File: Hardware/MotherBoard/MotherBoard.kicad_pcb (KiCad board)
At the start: 2 copper layers, 145 x 160 mm, 55 parts, among them J1 POWER, J10 I/O_PWR, J11 DMA_PULLUP, J12 NMI_PULLUP, J13 USB_OTG, J14 IRQ0_PULLUP, J2 I/O0, J3 ISA1, J4 ISA0, J5 I/O1, J6 EXTRN_CLCK, J9 Conn_02x02_Odd_Even, SW1 RESET_SW, SW2 ON_OFF, U1 AMS1117-5.0, U10 74HC245, U11 74HC245, U12 74HC245, U13 74HC541, U14 74HC541, U2 AT28C256, U3 WD65C22, U4 AS6C62256, U5 WD65C02, U6 74HC148, U7 74HC574, U8 ATF22V10B, U9 74HC245, X1 ACO-1MHz

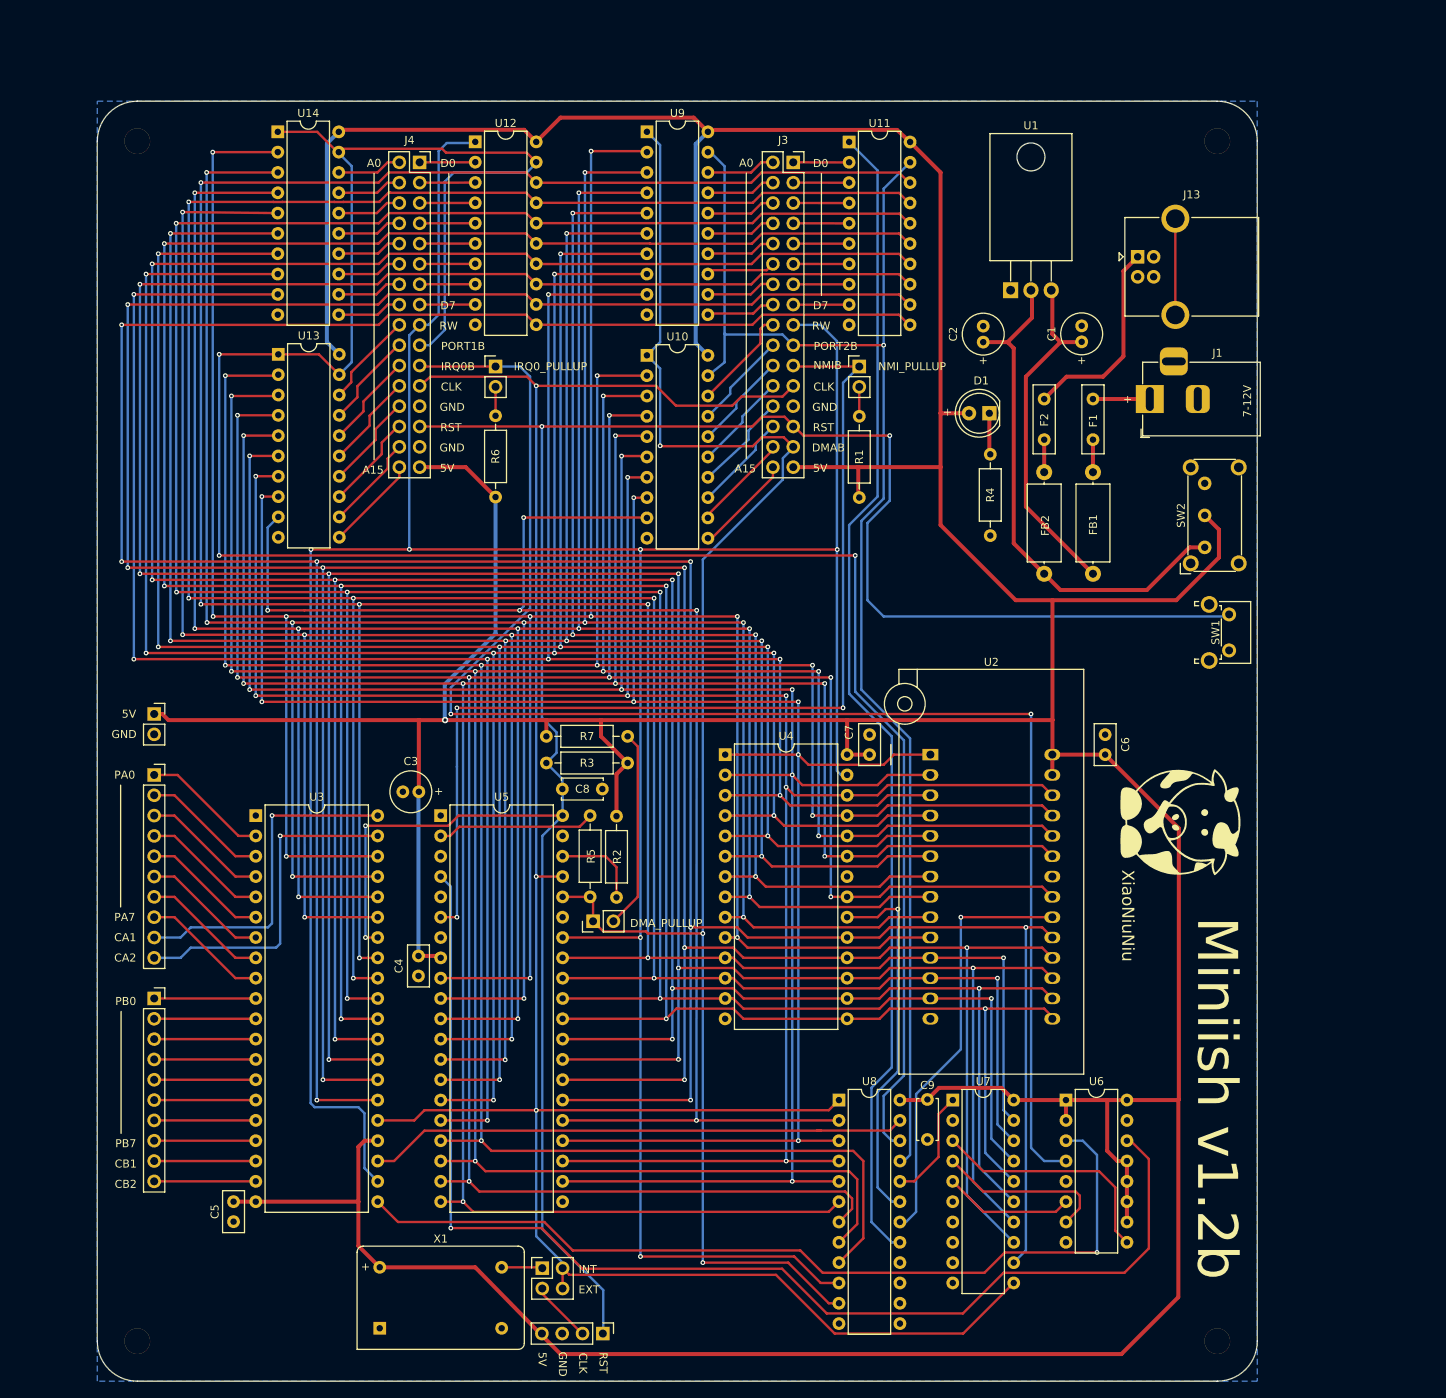
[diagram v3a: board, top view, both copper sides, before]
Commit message: Fix Reset, WAI Signal, Add PROG jumper and reformat luc files
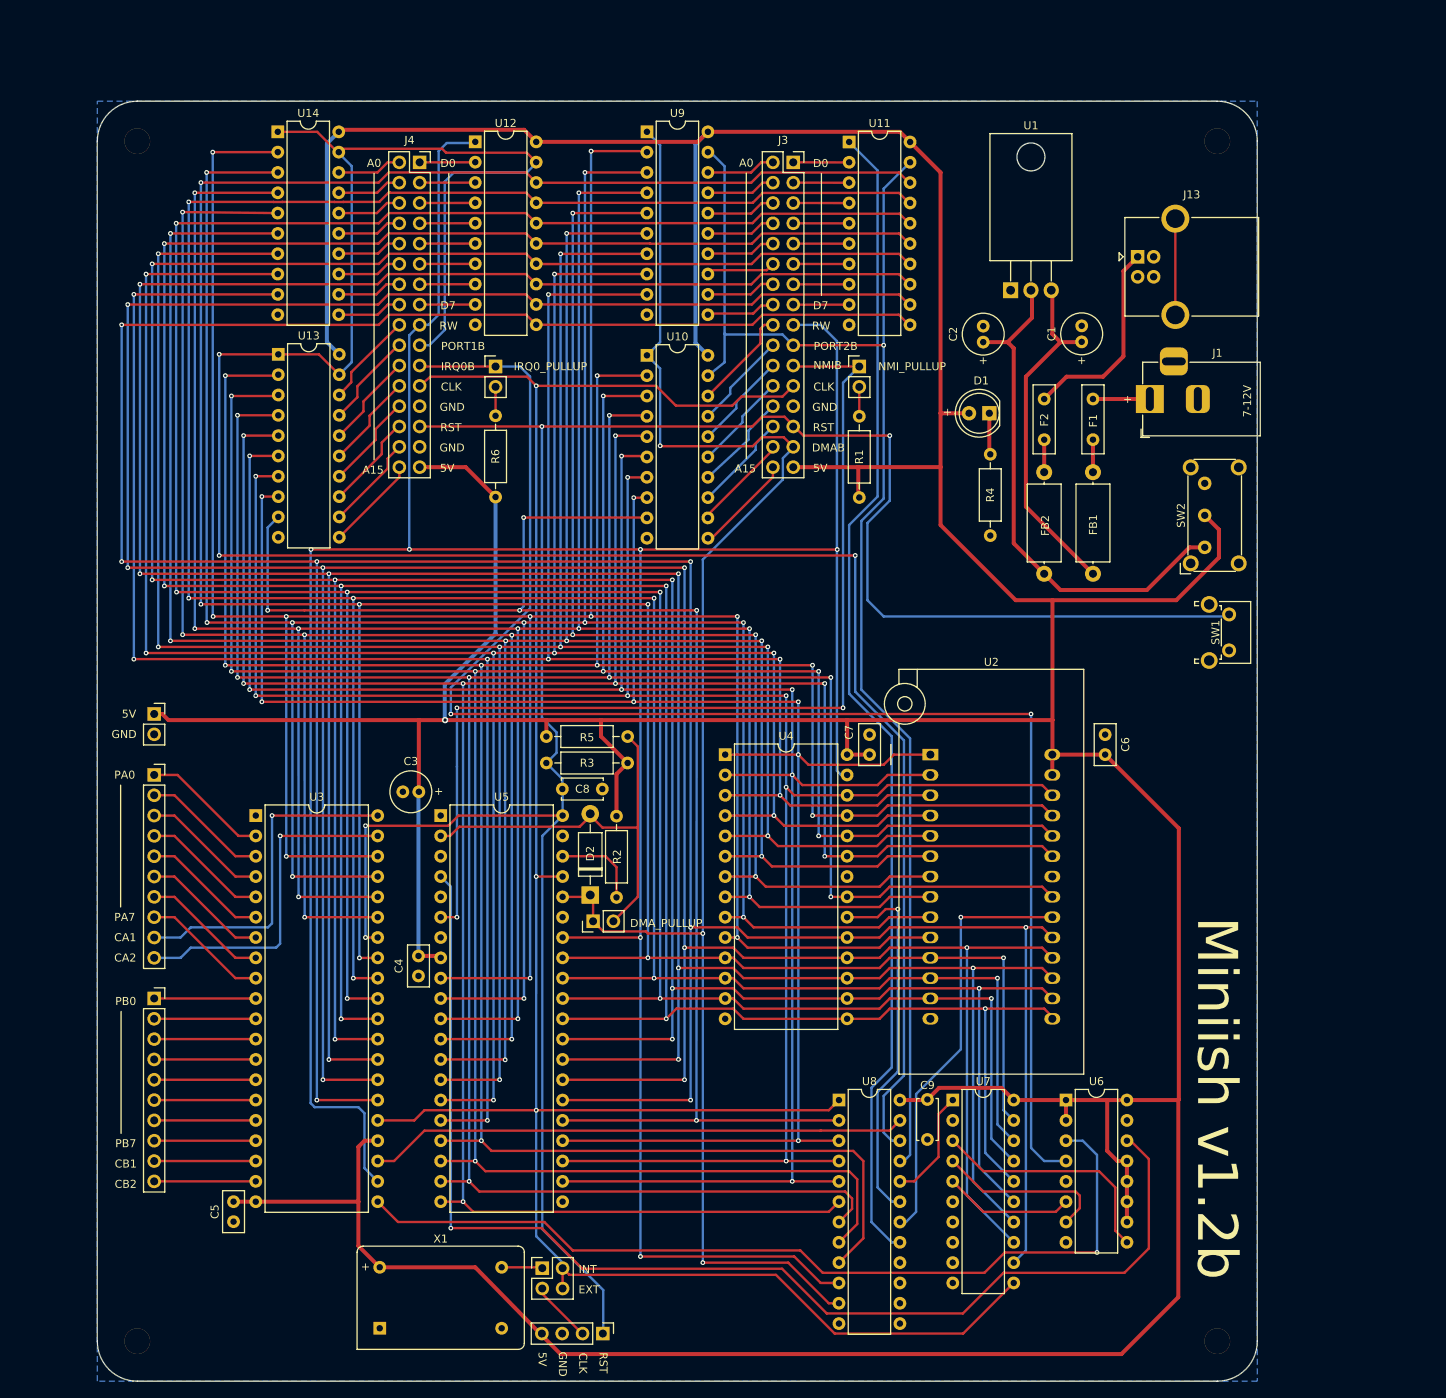
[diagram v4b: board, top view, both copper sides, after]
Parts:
- removed R7: 10K, Resistor_THT:R_Axial_DIN0207_L6.3mm_D2.5mm_P10.16mm_Horizontal
- removed XiaoNiuNiu: LOGO, Logos:SmallCow
- added D2: 1N4001, Diode_THT:D_DO-41_SOD81_P10.16mm_Horizontal, F.Cu at (84.8, 124.4)
- R1, R2, R5, R6: value 10K -> 3K3
- moved R5 10.9 mm to (89.5, 104.6), turned to 180 degrees
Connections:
- net /DMARW renamed /North Bridge/DMARW
- net /IOCSB renamed /Main /IOCSB
- net /IRQ0B renamed /North Bridge/IRQ0B
- net /IRQ1B renamed /Main /IRQ1B
- net /IRQB renamed /Main /IRQB
- net /NMIB renamed /Main /NMIB
- net /PORT1B renamed /North Bridge/PORT1B
- net /PORT2B renamed /North Bridge/PORT2B
- net /RAMCSB renamed /Main /RAMCSB
- net /ROMCSB renamed /Main /ROMCSB
- net /RW renamed /Main /RW
- J11 pad 1: /DMAB -> /Main /DMAB
- J11 pad 2: Net-(J11-Pad2) -> /Main /RDY
- J13 pad 2: (no net) -> unconnected-(J13-Pad2)
- J13 pad 3: (no net) -> unconnected-(J13-Pad3)
- J13 pad 5: no_connect_129 -> unconnected-(J13-Pad5)
- J3 pad 15: /DMAB -> /Main /DMAB
- R5 pad 1: Net-(R5-Pad1) -> /Main /RDY
- R5 pad 2: /DMAB -> +5V
- U10 pad 1: /DMAB -> /Main /DMAB
- U5 pad 1: (no net) -> unconnected-(U5-Pad1)
- U5 pad 2: Net-(R5-Pad1) -> /Main /RDY
- U5 pad 3: (no net) -> unconnected-(U5-Pad3)
- U5 pad 35: (no net) -> unconnected-(U5-Pad35)
- U5 pad 36: /DMAB -> /Main /DMAB
- U5 pad 39: (no net) -> unconnected-(U5-Pad39)
- U5 pad 5: (no net) -> unconnected-(U5-Pad5)
- U5 pad 7: (no net) -> unconnected-(U5-Pad7)
- U6 pad 15: (no net) -> unconnected-(U6-Pad15)
- U8 pad 11: /DMAB -> /Main /DMAB
- U8 pad 14: (no net) -> unconnected-(U8-Pad14)
- U8 pad 15: (no net) -> unconnected-(U8-Pad15)
- U8 pad 16: (no net) -> unconnected-(U8-Pad16)
- U9 pad 1: /DMAB -> /Main /DMAB
- X1 pad 1: (no net) -> unconnected-(X1-Pad1)
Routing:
- net /Main /DMAB: track 0.00 -> 205.7 mm, vias 0 -> 3
- net /DMAB: track 205.7 -> 0.00 mm, vias 3 -> 0
- net /Main /RDY: track 0.00 -> 51.2 mm
- net Net-(J11-Pad2): track 24.9 -> 0.00 mm
- net Net-(R5-Pad1): track 19.7 -> 0.00 mm
- net unconnected-(J13-Pad5): track 0.00 -> 12.0 mm
- net no_connect_129: track 12.0 -> 0.00 mm
- net +5V: track 762.0 -> 760.2 mm

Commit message: Cleanup and update version
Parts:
- added XiaoNiuNiu: LOGO, Logos:SmallCow, F.Cu at (39.5, 176.1)
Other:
- board text added: "Miniish v1.2c"
- board text removed: "Miniish v1.2b"

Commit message: New motherboard version
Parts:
- removed J1: POWER, Connector_BarrelJack:BarrelJack_Horizontal
- removed J10: I/O_PWR, Connector_PinSocket_2.54mm:PinSocket_1x02_P2.54mm_Vertical
- removed J11: DMA_PULLUP, Connector_PinHeader_2.54mm:PinHeader_1x02_P2.54mm_Vertical
- removed J12: NMI_PULLUP, Connector_PinHeader_2.54mm:PinHeader_1x02_P2.54mm_Vertical
- removed J13: USB_OTG, Connector_USB:USB_B_OST_USB-B1HSxx_Horizontal
- removed J2: I/O0, Connector_PinSocket_2.54mm:PinSocket_1x10_P2.54mm_Vertical
- removed J5: I/O1, Connector_PinSocket_2.54mm:PinSocket_1x10_P2.54mm_Vertical
- removed J6: EXTRN_CLCK, Connector_PinHeader_2.54mm:PinHeader_1x04_P2.54mm_Vertical
- removed J9: Conn_02x02_Odd_Even, Connector_PinHeader_2.54mm:PinHeader_2x02_P2.54mm_Vertical
- removed SW1: RESET_SW, Button_Switch_THT:SW_Tactile_SPST_Angled_PTS645Vx83-2LFS
- removed SW2: ON_OFF, Button_Switch_THT:SW_E-Switch_EG1224_SPDT_Angled
- removed U10, U11, U12: 74HC245, Package_DIP:DIP-20_W7.62mm
- removed U13, U14: 74HC541, Package_DIP:DIP-20_W7.62mm
- removed X1: ACO-1MHz, Oscillator:Oscillator_DIP-14
- removed the XiaoNiuNiu at (39.5, 176.1)
- added +12V: POWER, Connector_BarrelJack:BarrelJack_Horizontal, F.Cu at (147.7, 28.8)
- added +5V: USB_OTG, Connector_USB:USB_B_OST_USB-B1HSxx_Horizontal, F.Cu at (161.6, 30.7)
- added 16MHz: ACO-16MHz, Oscillator:Oscillator_DIP-14, F.Cu at (40.3, 144.7)
- added C10: 100nF, Capacitor_THT:C_Disc_D5.0mm_W2.5mm_P2.50mm, F.Cu at (55.6, 101.6)
- added C11: 100nF, Capacitor_THT:C_Disc_D5.0mm_W2.5mm_P2.50mm, F.Cu at (86.7, 172.0)
- added C12: 100nF, Capacitor_THT:C_Disc_D5.0mm_W2.5mm_P2.50mm, F.Cu at (152.7, 172.0)
- added ClOCK_DIV: CLOCK_DIV, Button_Switch_THT:SW_DIP_SPSTx05_Slide_6.7x14.26mm_W7.62mm_P2.54mm_LowProfile, F.Cu at (39.7, 112.4)
- added DMAB: DMA_PULLUP, Connector_PinHeader_2.54mm:PinHeader_1x02_P2.54mm_Vertical, F.Cu at (131.1, 73.0)
- added IRQ2B: IRQ2_PULLUP, Connector_PinHeader_2.54mm:PinHeader_1x02_P2.54mm_Vertical, F.Cu at (42.9, 104.0)
- added IRQ3B: IRQ3_PULLUP, Connector_PinHeader_2.54mm:PinHeader_1x02_P2.54mm_Vertical, F.Cu at (21.3, 55.8)
- added IRQ4B: IRQ4_PULLUP, Connector_PinHeader_2.54mm:PinHeader_1x02_P2.54mm_Vertical, F.Cu at (39.1, 55.8)
- added IRQ5B: IRQ5_PULLUP, Connector_PinHeader_2.54mm:PinHeader_1x02_P2.54mm_Vertical, F.Cu at (56.8, 55.8)
- added IRQ6B: IRQ6_PULLUP, Connector_PinHeader_2.54mm:PinHeader_1x02_P2.54mm_Vertical, F.Cu at (74.6, 55.8)
- added J16: PORT2, NESConnector:NES_Cartdrige, F.Cu at (46.7, 56.5)
- added J17: PORT2, NESConnector:NES_Cartdrige, F.Cu at (64.5, 56.5)
- added J18: PORT3, NESConnector:NES_Cartdrige, F.Cu at (82.2, 56.5)
- added J19: GPIO1, Connector_PinSocket_2.54mm:PinSocket_1x10_P2.54mm_Vertical, F.Cu at (28.3, 179.7)
- added J20: GPIO2, Connector_PinSocket_2.54mm:PinSocket_1x10_P2.54mm_Vertical, F.Cu at (56.2, 179.7)
- added J21: GPIO1_PWR, Connector_PinSocket_2.54mm:PinSocket_1x02_P2.54mm_Vertical, F.Cu at (84.2, 179.7)
- added J22: GPIO3, Connector_PinSocket_2.54mm:PinSocket_1x10_P2.54mm_Vertical, F.Cu at (94.3, 179.7)
- added J23: GPIO4, Connector_PinSocket_2.54mm:PinSocket_1x10_P2.54mm_Vertical, F.Cu at (122.2, 179.7)
- added J24: GPIO2_PWR, Connector_PinSocket_2.54mm:PinSocket_1x02_P2.54mm_Vertical, F.Cu at (150.2, 179.7)
- added NIMB: NMI_PULLUP, Connector_PinHeader_2.54mm:PinHeader_1x02_P2.54mm_Vertical, F.Cu at (131.1, 65.4)
- added ON/OFF: ON_OFF, Button_Switch_THT:SW_E-Switch_EG1224_SPDT_Angled, F.Cu at (135.5, 20.7)
- added R10: 3K3, Resistor_THT:R_Axial_DIN0207_L6.3mm_D2.5mm_P10.16mm_Horizontal, F.Cu at (36.5, 65.4)
- added R7: 3K3, Resistor_THT:R_Axial_DIN0207_L6.3mm_D2.5mm_P10.16mm_Horizontal, F.Cu at (18.7, 65.4)
- added R8: 3K3, Resistor_THT:R_Axial_DIN0207_L6.3mm_D2.5mm_P10.16mm_Horizontal, F.Cu at (72.1, 65.4)
- added R9: 3K3, Resistor_THT:R_Axial_DIN0207_L6.3mm_D2.5mm_P10.16mm_Horizontal, F.Cu at (54.3, 65.4)
- added RESET: RESET_SW, Button_Switch_THT:SW_Tactile_SPST_Angled_PTS645Vx83-2LFS, F.Cu at (115.2, 18.4)
- added XiaoNiuNiu: LOGO, Cow:SmallCow, F.Cu at (158.6, 151.2)
- C1: value 10uF -> 10nF; footprint Capacitor_THT:C_Radial_D5.0mm_H11.0mm_P2.00mm -> Capacitor_THT:C_Disc_D5.0mm_W2.5mm_P2.50mm
- C2: value 22uF -> 10uF
- C3: value 10uF -> 22uF
- C4: value 100nF -> 470nF; footprint Capacitor_THT:C_Disc_D5.0mm_W2.5mm_P2.50mm -> Capacitor_THT:C_Disc_D5.0mm_W2.5mm_P5.00mm
- C5: value 100nF -> 10uF; footprint Capacitor_THT:C_Disc_D5.0mm_W2.5mm_P2.50mm -> Capacitor_THT:C_Radial_D5.0mm_H11.0mm_P2.00mm
- C8: value 470nF -> 220nF; footprint Capacitor_THT:C_Disc_D5.0mm_W2.5mm_P5.00mm -> Capacitor_THT:C_Disc_D5.0mm_W2.5mm_P2.50mm
- C9: value 220nF -> 100nF; footprint Capacitor_THT:C_Disc_D5.0mm_W2.5mm_P5.00mm -> Capacitor_THT:C_Disc_D5.0mm_W2.5mm_P2.50mm
- J14: value IRQ0_PULLUP -> PORT1; footprint Connector_PinHeader_2.54mm:PinHeader_1x02_P2.54mm_Vertical -> NESConnector:NES_Cartdrige
- J3: value ISA1 -> CLOCK_SEL; footprint Connector_PinSocket_2.54mm:PinSocket_2x16_P2.54mm_Vertical -> Connector_PinHeader_2.54mm:PinHeader_2x02_P2.54mm_Vertical
- J4: value ISA0 -> EXTRN_CLCK; footprint Connector_PinSocket_2.54mm:PinSocket_2x16_P2.54mm_Vertical -> Connector_PinHeader_2.54mm:PinHeader_1x04_P2.54mm_Vertical
- R1: value 3K3 -> 220
- R4: value 220 -> 3K3
- U1: value AMS1117-5.0 -> 74HC590A; footprint Package_TO_SOT_THT:TO-220-3_Horizontal_TabDown -> Package_DIP:DIP-16_W7.62mm
- U2: value AT28C256 -> AMS1117-5.0; footprint Socket:DIP_Socket-28_W11.9_W12.7_W15.24_W17.78_W18.5_3M_228-1277-00-0602J -> Package_TO_SOT_THT:TO-220-3_Horizontal_TabDown
- U3: value WD65C22 -> AS6C62256; footprint Package_DIP:DIP-40_W15.24mm -> Package_DIP:DIP-28_W15.24mm
- U4: value AS6C62256 -> WD65C02; footprint Package_DIP:DIP-28_W15.24mm -> Package_DIP:DIP-40_W15.24mm
- U5: value WD65C02 -> 74HC148; footprint Package_DIP:DIP-40_W15.24mm -> Package_DIP:DIP-16_W7.62mm
- U6: value 74HC148 -> 74HC574; footprint Package_DIP:DIP-16_W7.62mm -> Package_DIP:DIP-20_W7.62mm
- U7: value 74HC574 -> ATF22V10B; footprint Package_DIP:DIP-20_W7.62mm -> Package_DIP:DIP-24_W7.62mm
- U8: value ATF22V10B -> WD65C22; footprint Package_DIP:DIP-24_W7.62mm -> Package_DIP:DIP-40_W15.24mm
- U9: value 74HC245 -> WD65C22; footprint Package_DIP:DIP-20_W7.62mm -> Package_DIP:DIP-40_W15.24mm
- moved H2 150.3 mm to (178.1, 19.6)
- moved H3 149.9 mm to (178.1, 179.6)
- moved J3 147.3 mm to (23.2, 151.7)
- moved H1 145.5 mm to (18.1, 19.6)
- moved H4 145.1 mm to (18.1, 179.6)
- moved U9 143.2 mm to (99.4, 172.0), turned to 90 degrees
- moved U1 142.9 mm to (19.4, 129.5)
- moved C1 137.9 mm to (27.0, 124.4), turned to 180 degrees
- moved J4 127.2 mm to (18.1, 151.7)
- moved U3 117.5 mm to (156.5, 84.4)
- moved C5 108.7 mm to (125.3, 95.2), turned to 0 degrees
- moved C3 103.3 mm to (144.5, 47.6), turned to 90 degrees
- moved C4 97.7 mm to (146.3, 80.6), turned to 180 degrees
- moved U6 94.6 mm to (61.3, 104.7)
- moved U8 85.4 mm to (33.4, 172.0), turned to 90 degrees
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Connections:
- C1 pad 1: Net-(C1-Pad1) -> +5V
- C2 pad 1: Net-(C2-Pad1) -> Net-(#FLG01-pwr)
- C3 pad 1: +5V -> Net-(SW2-A)
- C4 pad 1: +5V -> RESET
- C8 pad 1: RESET -> +5V
- D1 pad 1: Net-(D1-Pad1) -> Net-(D1-K)
- D2 pad 1: /Main /DMAB -> /North Bridge/DMAB
- D2 pad 2: /Main /RDY -> /North Bridge/RDY
- FB1 pad 2: Net-(C1-Pad1) -> Net-(SW2-A)
- FB2 pad 2: Net-(C2-Pad1) -> Net-(#FLG01-pwr)
- J14 pad 1: /North Bridge/IRQ0B -> GND
- J14 pad 2: Net-(J14-Pad2) -> +5V
- J3 pad 2: Net-(J3-Pad2) -> CLOCK
- J3 pad 3: Net-(J3-Pad3) -> ECLOCK
- J3 pad 4: Net-(J3-Pad4) -> CLOCK
- J4 pad 1: Net-(J4-Pad1) -> RESET
- J4 pad 2: Net-(J4-Pad2) -> ECLOCK
- J4 pad 3: Net-(J4-Pad3) -> GND
- J4 pad 4: Net-(J4-Pad4) -> +5V
- R1 pad 1: Net-(J12-Pad2) -> Net-(D1-K)
- R1 pad 2: +5V -> GND
- R2 pad 1: +5V -> Net-(J5-Pin_2)
- R2 pad 2: Net-(R2-Pad2) -> +5V
- R4 pad 1: Net-(D1-Pad1) -> /North Bridge/RDY
- R4 pad 2: GND -> +5V
- R5 pad 1: /Main /RDY -> +5V
- R5 pad 2: +5V -> /North Bridge/SOB
- R6 pad 1: Net-(J14-Pad2) -> Net-(J7-Pin_2)
- U1 pad 1: GND -> /4MHz
- U1 pad 2: Net-(C2-Pad1) -> /2MHz
- U1 pad 3: Net-(C1-Pad1) -> /1MHz
- U2 pad 1: /A14 -> GND
- U2 pad 2: /A12 -> Net-(SW2-A)
- U2 pad 3: /A7 -> Net-(#FLG01-pwr)
- U3 pad 1: GND -> /GPIO/A14
- U3 pad 10: PB0 -> /GPIO/A0
- U3 pad 11: PB1 -> /GPIO/D0
- U3 pad 12: PB2 -> /GPIO/D1
- U3 pad 13: PB3 -> /GPIO/D2
- U3 pad 14: PB4 -> GND
- U3 pad 15: PB5 -> /GPIO/D3
- U3 pad 16: PB6 -> /GPIO/D4
- U3 pad 17: PB7 -> /GPIO/D5
- U3 pad 18: CB1 -> /GPIO/D6
- U3 pad 19: CB2 -> /GPIO/D7
- U3 pad 2: PA0 -> /GPIO/A12
- U3 pad 20: +5V -> /North Bridge/RAMCSB
- U3 pad 21: /Main /IRQ1B -> /GPIO/A10
- U3 pad 22: /Main /RW -> GND
- U3 pad 23: /Main /IOCSB -> /GPIO/A11
- U3 pad 24: +5V -> /GPIO/A9
- U3 pad 25: CLOCK -> /GPIO/A8
- U3 pad 26: /D7 -> /GPIO/A13
- U3 pad 27: /D6 -> /GPIO/RW
- U3 pad 28: /D5 -> +5V
- U3 pad 3: PA1 -> /GPIO/A7
- U3 pad 4: PA2 -> /GPIO/A6
- U3 pad 5: PA3 -> /GPIO/A5
- U3 pad 6: PA4 -> /GPIO/A4
- U3 pad 7: PA5 -> /GPIO/A3
- U3 pad 8: PA6 -> /GPIO/A2
- U3 pad 9: PA7 -> /GPIO/A1
- U4 pad 1: /A14 -> unconnected-(U4-~{VP}-Pad1)
- U4 pad 10: /A0 -> /GPIO/A1
- U4 pad 11: /D0 -> /GPIO/A2
- U4 pad 12: /D1 -> /GPIO/A3
- U4 pad 13: /D2 -> /GPIO/A4
- U4 pad 14: GND -> /GPIO/A5
- U4 pad 15: /D3 -> /GPIO/A6
- U4 pad 16: /D4 -> /GPIO/A7
- U4 pad 17: /D5 -> /GPIO/A8
- U4 pad 18: /D6 -> /GPIO/A9
- U4 pad 19: /D7 -> /GPIO/A10
- U4 pad 2: /A12 -> /North Bridge/RDY
- U4 pad 20: /Main /RAMCSB -> /GPIO/A11
- U4 pad 21: /A10 -> GND
- U4 pad 22: GND -> /GPIO/A12
- U4 pad 23: /A11 -> /GPIO/A13
- U4 pad 24: /A9 -> /GPIO/A14
- U4 pad 25: /A8 -> /GPIO/A15
- U4 pad 26: /A13 -> /GPIO/D7
- U4 pad 27: /Main /RW -> /GPIO/D6
- U4 pad 28: +5V -> /GPIO/D5
- U4 pad 3: /A7 -> unconnected-(U4-PHI1out-Pad3)
- U4 pad 4: /A6 -> /North Bridge/IRQB
- U4 pad 5: /A5 -> unconnected-(U4-~{ML}-Pad5)
- U4 pad 6: /A4 -> /North Bridge/NMIB
- U4 pad 7: /A3 -> unconnected-(U4-SYNC-Pad7)
- U4 pad 8: /A2 -> +5V
- U4 pad 9: /A1 -> /GPIO/A0
- U5 pad 1: unconnected-(U5-Pad1) -> /Ports/IRQ3B
- U5 pad 10: /A1 -> +5V
- U5 pad 11: /A2 -> /Ports/IRQ6B
- U5 pad 12: /A3 -> /Ports/IRQ5B
- U5 pad 13: /A4 -> /Ports/IRQ4B
- U5 pad 14: /A5 -> /North Bridge/IRQB
- U5 pad 15: /A6 -> unconnected-(U5-EO-Pad15)
- U5 pad 16: /A7 -> +5V
- U5 pad 2: /Main /RDY -> /Ports/IRQ2B
- U5 pad 3: unconnected-(U5-Pad3) -> /GPIO/IRQ1B
- U5 pad 4: /Main /IRQB -> /GPIO/IRQ0B
- U5 pad 5: unconnected-(U5-Pad5) -> GND
- U5 pad 6: /Main /NMIB -> Net-(U5-S2)
- U5 pad 7: unconnected-(U5-Pad7) -> Net-(U5-S1)
- U5 pad 8: +5V -> GND
- U5 pad 9: /A0 -> Net-(U5-S0)
- U6 pad 1: +5V -> Net-(U6-OE)
- U6 pad 10: +5V -> GND
- U6 pad 11: +5V -> CLOCK
- U6 pad 12: +5V -> /GPIO/D7
- U6 pad 13: +5V -> /GPIO/D6
- U6 pad 14: /Main /IRQB -> /GPIO/D5
- U6 pad 15: unconnected-(U6-Pad15) -> /GPIO/D4
- U6 pad 16: +5V -> /GPIO/D3
- U6 pad 2: +5V -> GND
- U6 pad 3: /Main /IRQ1B -> Net-(U5-S0)
- U6 pad 4: /North Bridge/IRQ0B -> Net-(U5-S1)
- U6 pad 5: GND -> Net-(U5-S2)
- U6 pad 6: Net-(U6-Pad6) -> GND
- U6 pad 7: Net-(U6-Pad7) -> GND
- U6 pad 9: Net-(U6-Pad9) -> GND
- U7 pad 1: Net-(U7-Pad1) -> CLOCK
- U7 pad 10: GND -> /North Bridge/DMAB
- U7 pad 11: CLOCK -> GND
- U7 pad 12: /D7 -> GND
- U7 pad 13: /D6 -> GND
- U7 pad 14: /D5 -> unconnected-(U7-O9-Pad14)
- U7 pad 15: /D4 -> /North Bridge/RAMCSB
- U7 pad 16: /D3 -> /Ports/ROMCSB
- U7 pad 17: /D2 -> /Ports/PORT1CSB
- U7 pad 18: /D1 -> /Ports/PORT2CSB
- U7 pad 19: /D0 -> /Ports/PORT3CSB
- U7 pad 2: GND -> /GPIO/A15
- U7 pad 20: +5V -> /GPIO/CIA1CSB
- U7 pad 3: Net-(U6-Pad9) -> /GPIO/A14
- U7 pad 4: Net-(U6-Pad7) -> /GPIO/A13
- U7 pad 5: Net-(U6-Pad6) -> /GPIO/A12
- U7 pad 6: GND -> /GPIO/A11
- U7 pad 7: GND -> /GPIO/A10
- U7 pad 8: GND -> /GPIO/A9
- U7 pad 9: GND -> /GPIO/A8
- U8 pad 1: CLOCK -> GND
- U8 pad 10: /Main /RW -> PB10
- U8 pad 11: /Main /DMAB -> PB11
- U8 pad 12: GND -> PB12
- U8 pad 13: GND -> PB13
- U8 pad 14: unconnected-(U8-Pad14) -> PB14
- U8 pad 15: unconnected-(U8-Pad15) -> PB15
- U8 pad 16: unconnected-(U8-Pad16) -> PB16
- U8 pad 17: /North Bridge/DMARW -> PB17
- U8 pad 18: /Main /ROMCSB -> CB11
- U8 pad 19: /Main /RAMCSB -> CB12
- U8 pad 2: /A15 -> PA10
- U8 pad 20: Net-(U7-Pad1) -> +5V
- U8 pad 21: /North Bridge/PORT2B -> /GPIO/IRQ0B
- U8 pad 22: /North Bridge/PORT1B -> /GPIO/RW
- U8 pad 23: /Main /IOCSB -> /GPIO/CIA1CSB
- U8 pad 3: /A14 -> PA11
- U8 pad 4: /A13 -> PA12
- U8 pad 5: /A12 -> PA13
- U8 pad 6: /A11 -> PA14
- U8 pad 7: /A10 -> PA15
- U8 pad 8: /A9 -> PA16
- U8 pad 9: /A8 -> PA17
- U9 pad 1: /Main /DMAB -> GND
- U9 pad 10: GND -> PB20
- U9 pad 11: Net-(J3-Pad24) -> PB21
- U9 pad 12: Net-(J3-Pad23) -> PB22
- U9 pad 13: Net-(J3-Pad22) -> PB23
- U9 pad 14: Net-(J3-Pad21) -> PB24
- U9 pad 15: Net-(J3-Pad20) -> PB25
- U9 pad 16: Net-(J3-Pad19) -> PB26
- U9 pad 17: Net-(J3-Pad18) -> PB27
- U9 pad 18: Net-(J3-Pad17) -> CB21
- U9 pad 19: /North Bridge/PORT2B -> CB22
- U9 pad 2: /A0 -> PA20
- U9 pad 3: /A1 -> PA21
- U9 pad 4: /A2 -> PA22
- U9 pad 5: /A3 -> PA23
- U9 pad 6: /A4 -> PA24
- U9 pad 7: /A5 -> PA25
- U9 pad 8: /A6 -> PA26
- U9 pad 9: /A7 -> PA27
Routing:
- net /D7: track 448.8 -> 0.00 mm, vias 8 -> 0
- net /D6: track 439.1 -> 0.00 mm, vias 8 -> 0
- net /D5: track 426.1 -> 0.00 mm, vias 8 -> 0
- net /D4: track 412.6 -> 0.00 mm, vias 8 -> 0
- net /D3: track 399.8 -> 0.00 mm, vias 7 -> 0
- net /Main /RW: track 393.4 -> 0.00 mm, vias 6 -> 0
- net /GPIO/A9: track 0.00 -> 391.9 mm, vias 0 -> 5
- net /GPIO/A8: track 0.00 -> 389.9 mm, vias 0 -> 5
- net /GPIO/A10: track 0.00 -> 385.7 mm, vias 0 -> 5
- net /D2: track 381.7 -> 0.00 mm, vias 7 -> 0
- net /GPIO/D3: track 0.00 -> 375.9 mm, vias 0 -> 6
- net /GPIO/D7: track 0.00 -> 375.4 mm, vias 0 -> 7
- net /D1: track 374.4 -> 0.00 mm, vias 7 -> 0
- net /GPIO/D5: track 0.00 -> 374.2 mm, vias 0 -> 6
- net /GPIO/D6: track 0.00 -> 373.2 mm, vias 0 -> 6
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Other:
- board size 145 x 160 mm -> 170 x 170 mm
- board text added: "+5V"
- board text added: "."
- board text added: "16MHz"
- board text added: "1MHz"
- board text added: "2MHz"
- board text added: "4MHz"
- board text added: "8MHz"
- board text added: "A11"
- board text added: "A12"
- board text added: "Miniish v1.3"
- board text added: "RAMB"
- board text removed: "5V"
- board text removed: "7-12V"
- board text removed: "IRQ0B"
- board text removed: "Miniish v1.2c"
- board text removed: "PORT1B"
- board text removed: "PORT2B"

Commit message: Finalize 1.3
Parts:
- removed R5: 3K3, Resistor_THT:R_Axial_DIN0207_L6.3mm_D2.5mm_P10.16mm_Horizontal
- added R11: 3K3, Resistor_THT:R_Axial_DIN0207_L6.3mm_D2.5mm_P10.16mm_Horizontal, F.Cu at (126.1, 80.6)
- added R12: 3K3, Resistor_THT:R_Axial_DIN0207_L6.3mm_D2.5mm_P10.16mm_Horizontal, F.Cu at (151.5, 89.5)
- J10: renamed from IRQ5B; value IRQ5_PULLUP -> IRQ5
- J11: renamed from IRQ4B; value IRQ4_PULLUP -> IRQ4
- J17: value PORT2 -> PORT3
- J18: value PORT3 -> PORT4/ROM
- J2: renamed from +12V; value POWER -> POWER +12V
- J5: renamed from NIMB; value NMI_PULLUP -> NMI
- J6: renamed from DMAB; value DMA_PULLUP -> DMA
- J7: renamed from IRQ2B; value IRQ2_PULLUP -> IRQ2
- J8: renamed from IRQ3B; value IRQ3_PULLUP -> IRQ3
- J9: renamed from IRQ6B; value IRQ6_PULLUP -> IRQ6
- SW1: renamed from ClOCK_DIV; value CLOCK_DIV -> CLOCK_SPD
- SW3: renamed from RESET; value RESET_SW -> RESET
- moved J8 21.4 mm to (19.9, 77.2), turned to 0 degrees
- moved J10 21.3 mm to (54.9, 77.0), turned to 0 degrees
- moved J11 21.0 mm to (37.2, 76.8), turned to 0 degrees
- moved J9 21.0 mm to (72.7, 76.8), turned to 0 degrees
- moved R7 17.9 mm to (19.9, 83.3)
- moved R10 17.8 mm to (37.2, 83.1)
- moved R8 17.8 mm to (72.7, 83.1)
- moved R9 17.8 mm to (54.9, 83.1)
- moved R4 16.6 mm to (134.9, 66.6)
- moved XiaoNiuNiu 14.6 mm to (170.5, 159.6), turned to 90 degrees
- moved J5 10.4 mm to (131.1, 75.8), turned to 180 degrees
- moved R2 10.2 mm to (134.9, 71.7), turned to 0 degrees
- moved J6 7.63 mm to (130.9, 65.4)
- moved H3 6.71 mm to (175.1, 173.6)
- moved H4 6.08 mm to (17.1, 173.6)
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- renumbered +5V to J1, ON/OFF to SW2, 16MHz to X1
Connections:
- J6 pad 2: /North Bridge/RDY -> Net-(J6-Pin_2)
- R4 pad 1: /North Bridge/RDY -> Net-(J6-Pin_2)
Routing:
- net +5V: track 1034.7 -> 978.1 mm
- net /North Bridge/IRQB: track 142.2 -> 93.5 mm, vias 2 -> 1
- net Net-(J5-Pin_2): track 15.5 -> 4.44 mm
- net Net-(J10-Pin_2): track 9.53 -> 2.92 mm
- net Net-(J8-Pin_2): track 9.53 -> 3.43 mm
- net Net-(J9-Pin_2): track 9.53 -> 3.69 mm
- net Net-(J11-Pin_2): track 9.53 -> 3.82 mm
- net /GPIO/D0: track 370.9 -> 365.9 mm, vias 7 -> 8
- net /Ports/IRQ6B: track 103.1 -> 108.0 mm, vias 2 -> 3
- net /GPIO/D1: track 372.0 -> 367.4 mm, vias 7 -> 8
- net Net-(J6-Pin_2): track 0.00 -> 4.50 mm
- net /GPIO/D2: track 373.1 -> 368.9 mm, vias 7 -> 8
- net /GPIO/D5: track 374.2 -> 370.1 mm, vias 6 -> 7
- net /North Bridge/RDY: track 18.6 -> 14.7 mm
- net /GPIO/D3: track 375.9 -> 372.1 mm, vias 6 -> 7
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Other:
- board text added: "IRQB"
- board text added: "PORTB"

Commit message: Version 1.3
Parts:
- added C13: 100nF, Capacitor_THT:C_Disc_D5.0mm_W2.5mm_P2.50mm, F.Cu at (21.9, 151.7)
- C1: value 10nF -> 100nF
- SW2: value ON_OFF -> OFF_ON
- moved R3 69.6 mm to (93.0, 21.2)
- moved C4 69.3 mm to (110.8, 21.2)
- moved R11 9.12 mm to (134.9, 78.6)
- moved J3 4.10 mm to (24.7, 155.5), turned to -90 degrees
- moved R2 1.52 mm to (134.9, 73.2)
- moved R4 1.27 mm to (134.9, 67.9)
- moved R12 0.76 mm to (151.5, 88.7)
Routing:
- net +5V: track 978.1 -> 966.3 mm
- net /North Bridge/RDY: track 14.7 -> 25.1 mm
- net CLOCK: track 440.0 -> 441.5 mm
- net RESET: track 409.1 -> 408.1 mm
- net Net-(J5-Pin_2): track 4.44 -> 3.81 mm
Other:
- board text removed: "."
